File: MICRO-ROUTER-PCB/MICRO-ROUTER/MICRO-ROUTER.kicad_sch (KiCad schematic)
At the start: 15 parts, among them J1 Conn_01x02_Pin, J2 USB_A, P1 USB_C_Plug_USB2.0, SW1 SW_Push, SW2 8Devices Reset, SW3 UART Reset, U3 CP2102N-Axx-xQFN20

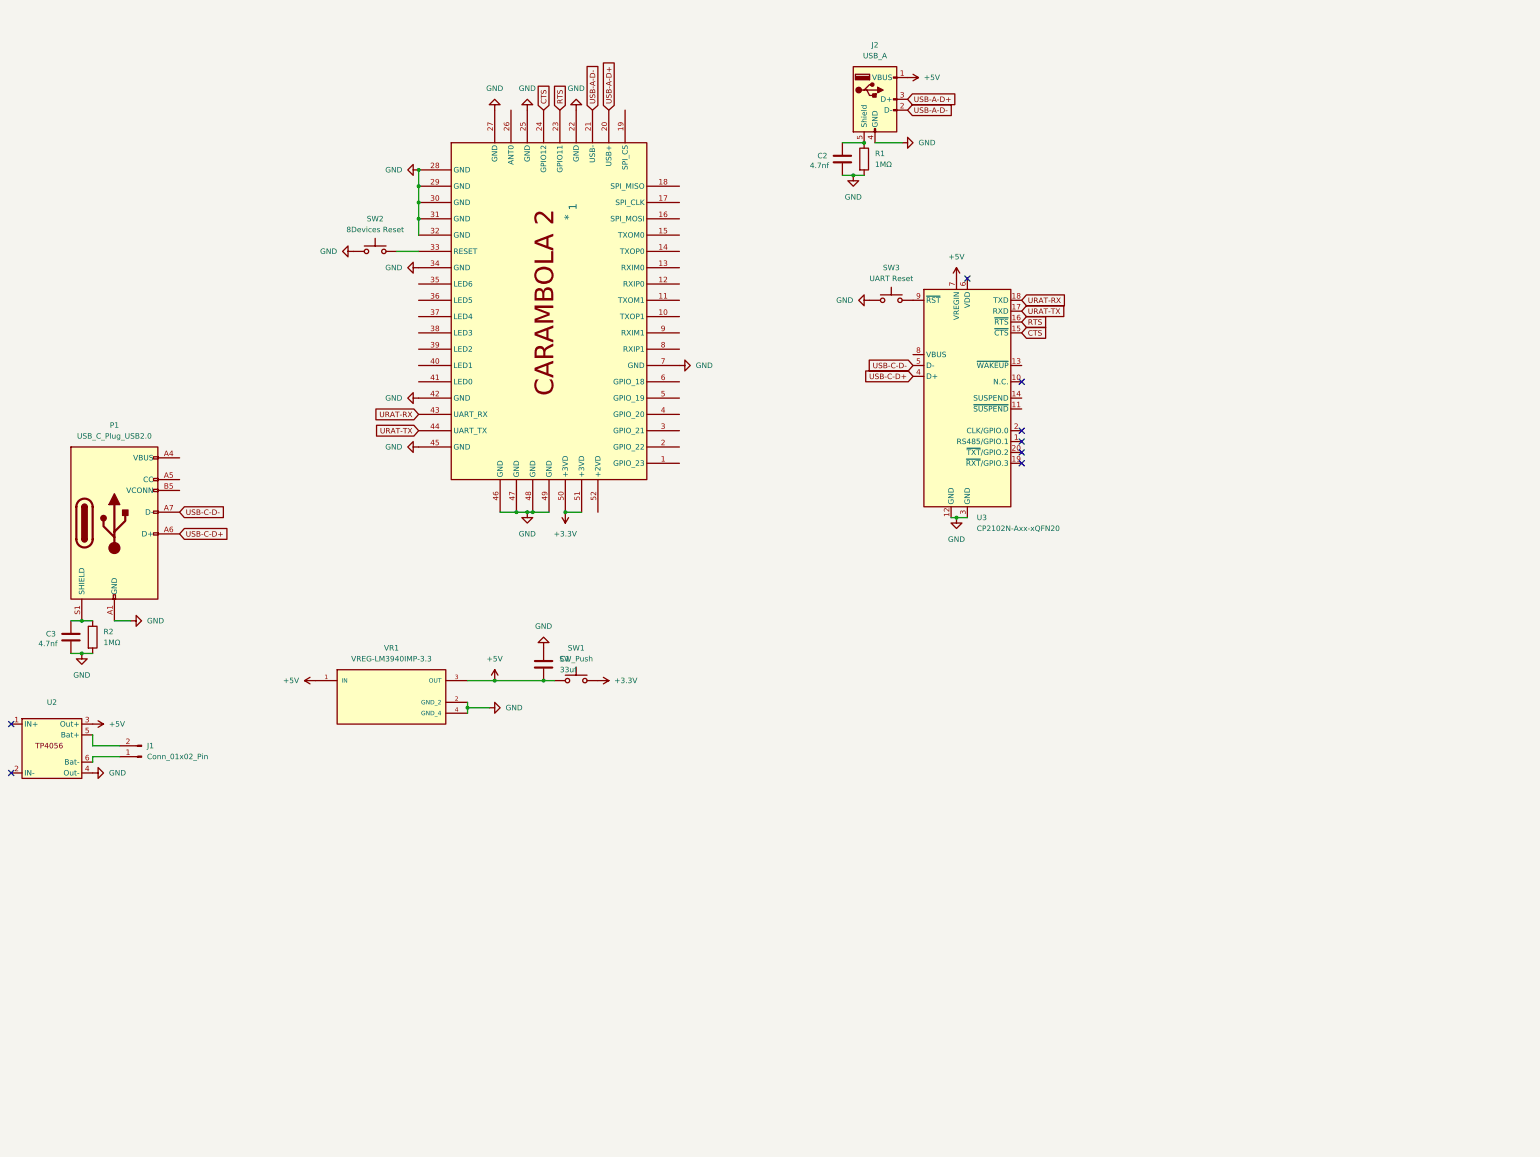
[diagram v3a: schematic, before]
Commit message: finished charger
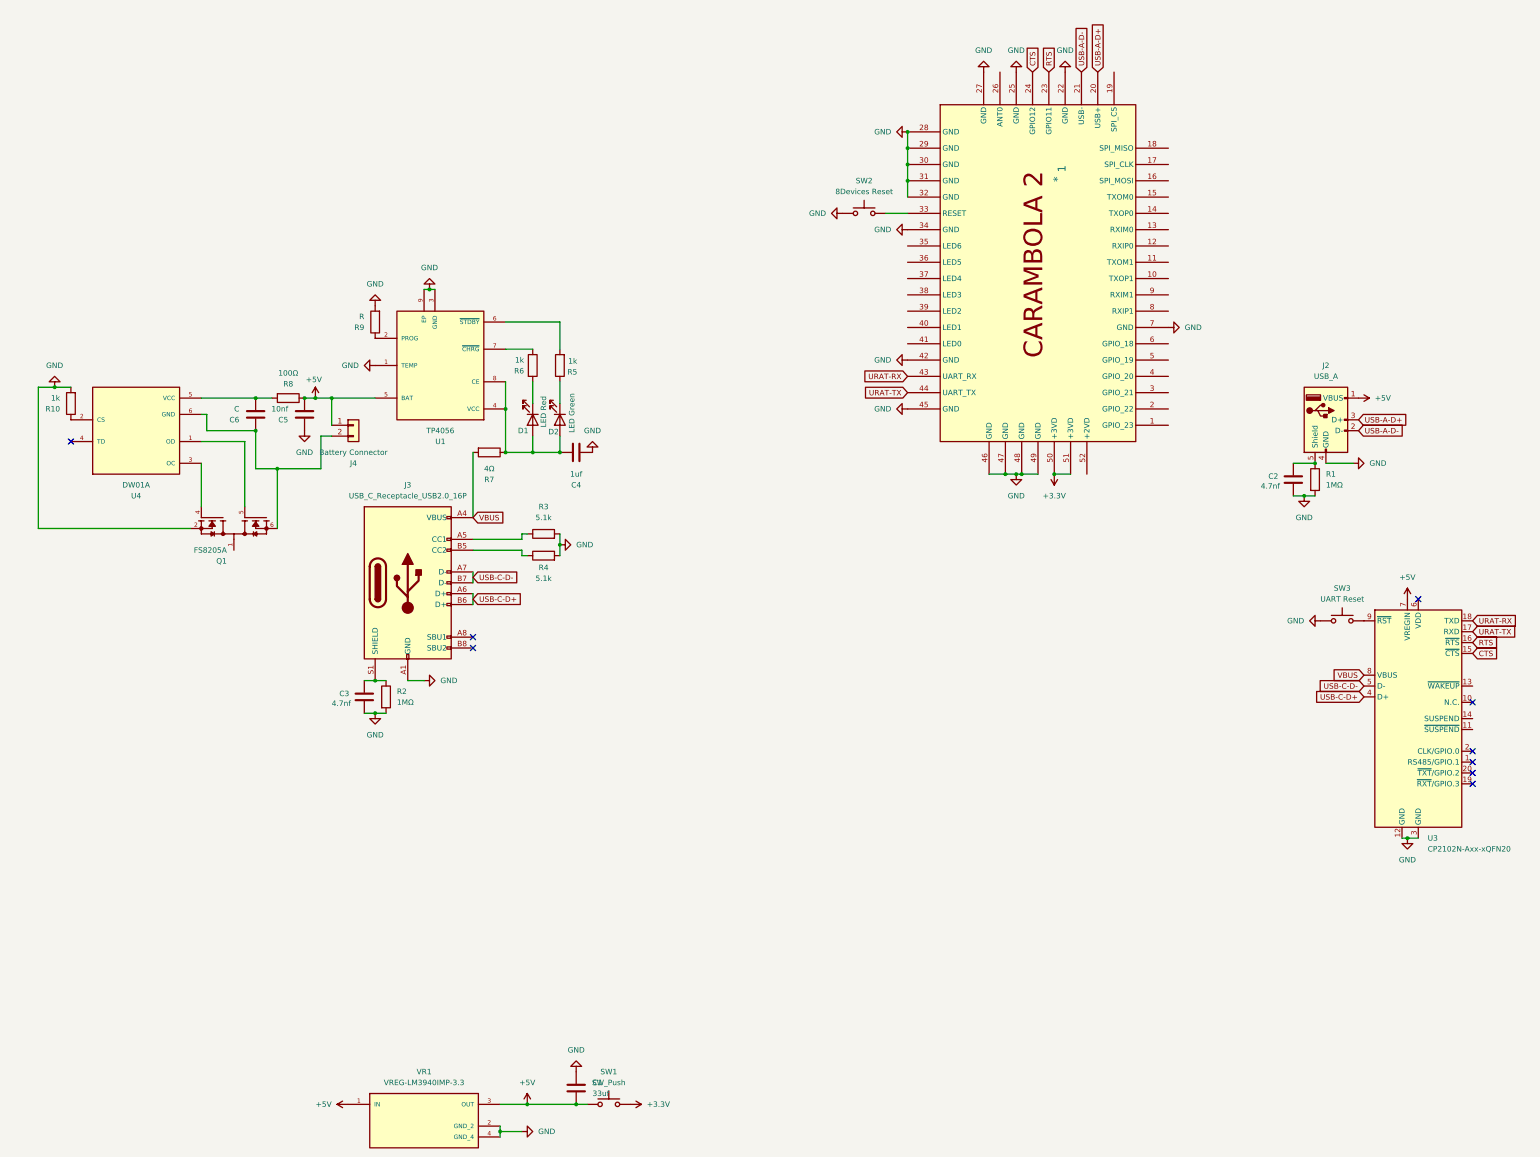
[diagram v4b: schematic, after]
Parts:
- removed J1: Conn_01x02_Pin, symbol Connector:Conn_01x02_Pin
- removed P1: USB_C_Plug_USB2.0, symbol Connector:USB_C_Plug_USB2.0
- removed U2: ~, symbol Custom Symbols:TP4056_Module
- added C4: 1uf, symbol Device:C
- added C5: 10nf, symbol Device:C
- added C6: C, symbol Device:C
- added D1: LED Red, symbol Device:LED
- added D2: LED Green, symbol Device:LED
- added J3: USB_C_Receptacle_USB2.0_16P, symbol Connector:USB_C_Receptacle_USB2.0_16P
- added J4: Battery Connector, symbol Connector_Generic:Conn_01x02
- added Q1: FS8205A, FS8205A:SOP65P640X120-8N, symbol Custom Symbols:FS8205A
- added R10, R5, R6: 1k, symbol Device:R
- added R3, R4: 5.1k, symbol Device:R
- added R7: 4Ω, symbol Device:R
- added R8: 100Ω, symbol Device:R
- added R9: R, symbol Device:R
- added U1: TP4056, symbol Custom Symbols:TP4056
- added U4: DW01A, DW01A:SOT95P280X145-6N, symbol Custom Symbols:DW01A
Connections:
- net +5V: now also C5.2, J4.1 (Pin_1), R8.1, U1.5 (BAT)
- net GND: now also C4.1, C5.1, J3.A1 (GND), J3.A12 (GND), J3.B1 (GND), J3.B12 (GND), Q1.2, R10.2, R3.2, R4.2, R9.2, U1.1 (TEMP), U1.3 (GND), U1.9 (EP)
- net USB-C-D+: now also J3.A6 (D+), J3.B6 (D+)
- net USB-C-D-: now also J3.A7 (D-), J3.B7 (D-)
- net VBUS: now reaches U3.8 (VBUS)
- net VBUS: now also J3.A4 (VBUS), J3.A9 (VBUS), J3.B4 (VBUS), J3.B9 (VBUS), R7.2
- net at C3.1, R2.1: now also J3.S1 (SHIELD)
- new net: J3.A5 (CC1), R3.1
- new net: J3.B5 (CC2), R4.1
- new net: D1.1 (K), R6.2
- new net: C4.2, D1.2 (A), D2.2 (A), R7.1, U1.4 (VCC), U1.8 (CE)
- new net: R6.1, U1.7 (~{CHRG})
- new net: C6.2, R8.2, U4.5 (VCC)
- new net: Q1.4, U4.3 (OC)
- new net: Q1.5, U4.1 (OD)
- new net: C6.1, J4.2 (Pin_2), Q1.6, U4.6 (GND)
- new net: R9.1, U1.2 (PROG)
- new net: R10.1, U4.2 (CS)
- new net: D2.1 (K), R5.1
- new net: R5.2, U1.6 (~{STDBY})
- no-connect marks 8 -> 9
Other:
- moved on the sheet: 1, C1, C2, C3, J2, R1, R2, SW1, SW2, SW3, U3, VR1
